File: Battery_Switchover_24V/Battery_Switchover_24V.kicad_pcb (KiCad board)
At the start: 2 copper layers, 188.9 x 89 mm, 102 parts, among them J1 USB_C_Receptacle_USB2.0_14P, J2 430450612, J4 430450612, J5 430450612, M1 Fan, Q1 PZT2222AT1G, SW1 SW_Push, U11 LM60CIM3, U12 L5973D, U13 AMS1117-3.3, U14 OPA2197xD, U2 ACS71240LLCBTR-010B3, U3 LPC11U14FBD48-201, U4 ACS37002, U5 ACS37002, U6 LM74610QDGKRQ1, U7 FDBL86066-F085, U8 ADS7830IPWR, Y1 12.000MHz

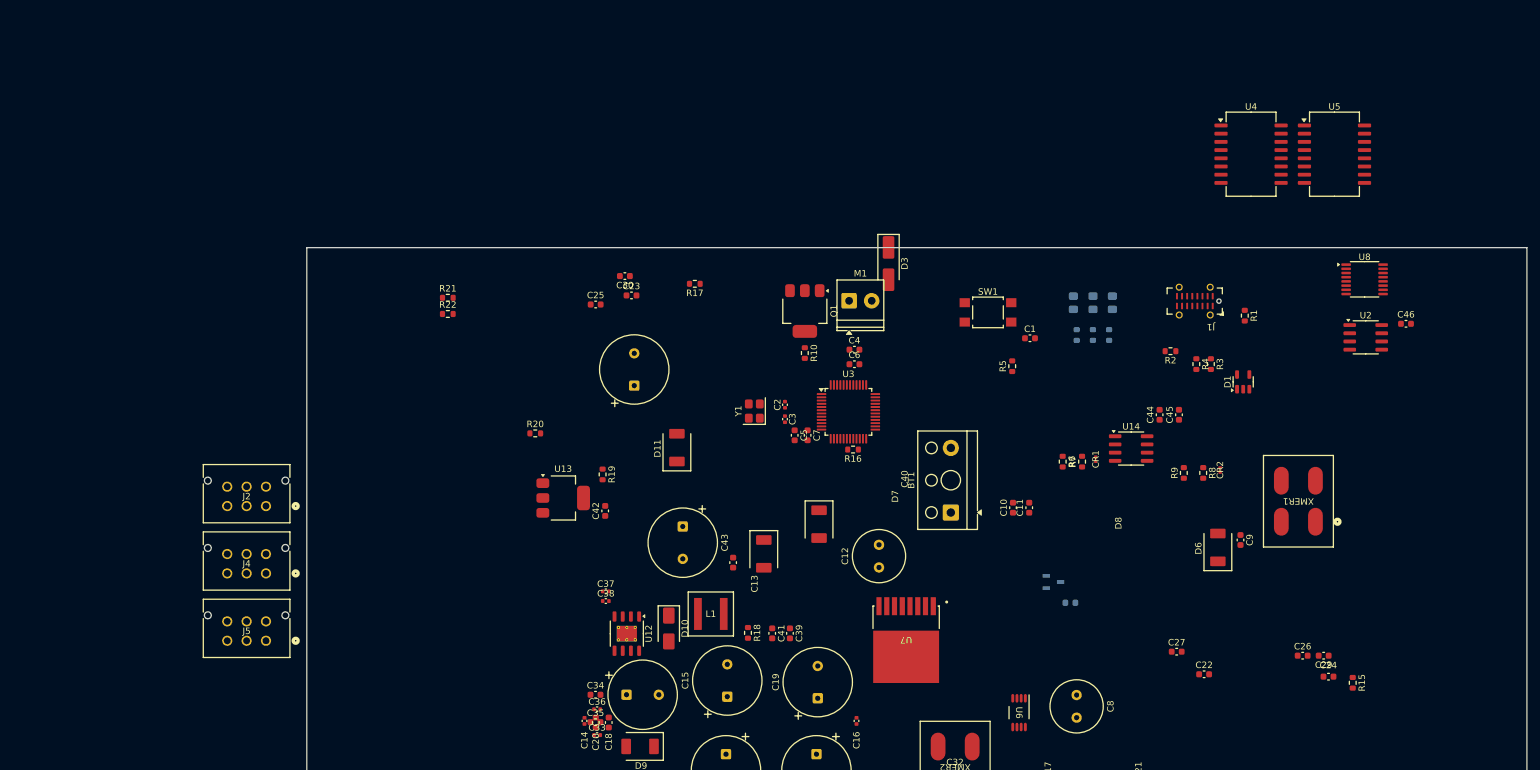
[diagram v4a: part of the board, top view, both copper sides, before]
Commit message: Batt current monitor IC added, batt moved to charger page
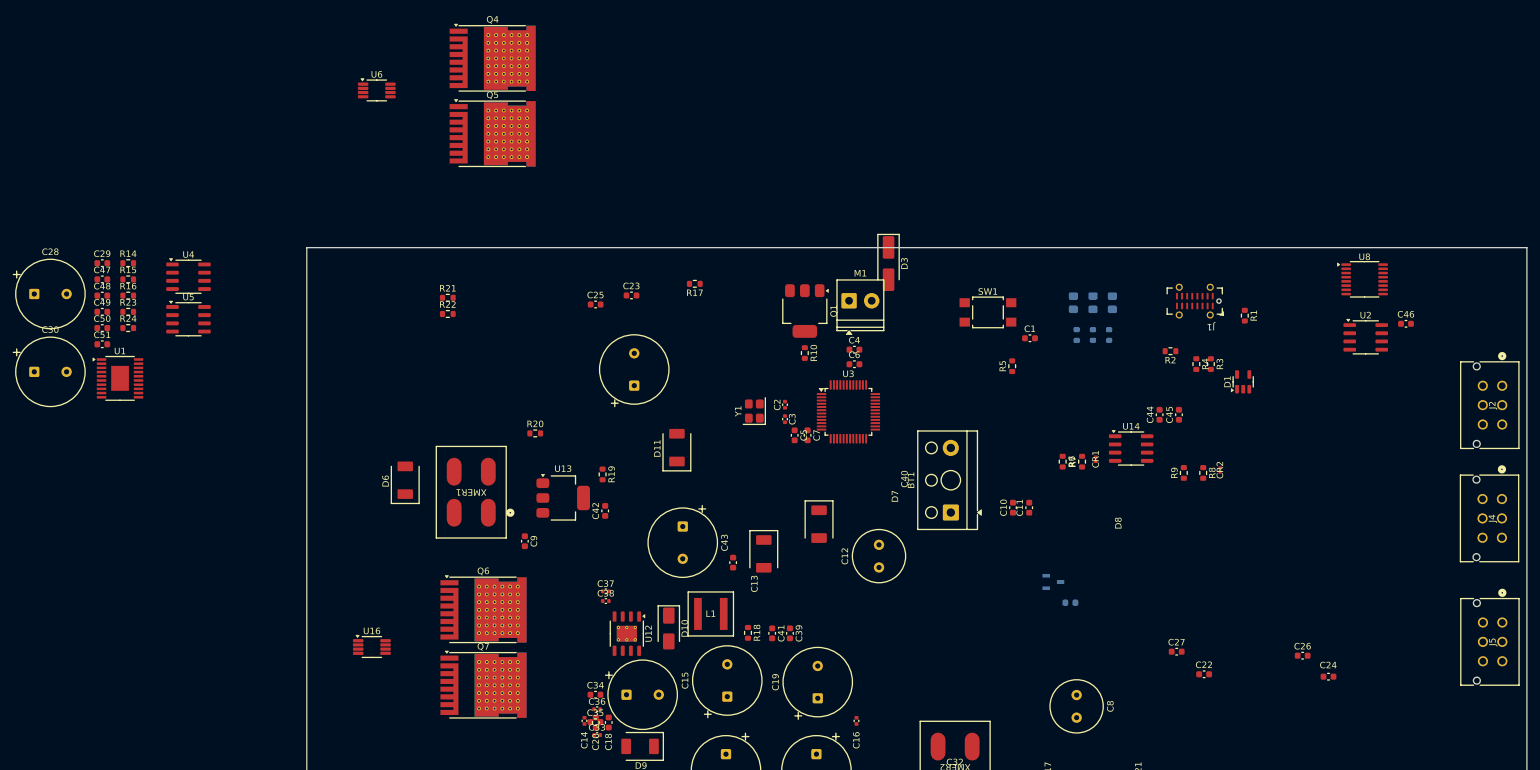
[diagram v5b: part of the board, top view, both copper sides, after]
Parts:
- removed U7: FDBL86066-F085, footprints:H-PSOF8L_ONS
- added C28: 330uF, Capacitor_THT:CP_Radial_Tantal_D10.5mm_P5.00mm, F.Cu at (47.1, 77.2)
- added C47: 100nF, Capacitor_SMD:C_0603_1608Metric, F.Cu at (57.7, 74.9)
- added C48: 100nF, Capacitor_SMD:C_0603_1608Metric, F.Cu at (57.7, 77.4)
- added C49: 100nF, Capacitor_SMD:C_0603_1608Metric, F.Cu at (57.7, 79.9)
- added C50: 100nF, Capacitor_SMD:C_0603_1608Metric, F.Cu at (57.7, 82.4)
- added C51: 100nF, Capacitor_SMD:C_0603_1608Metric, F.Cu at (57.7, 85.0)
- added Q4: FDBL86066-F085, Package_TO_SOT_SMD:Infineon_PG-HSOF-8-1_ThermalVias, F.Cu at (118.1, 40.7)
- added Q5: FDBL86066-F085, Package_TO_SOT_SMD:Infineon_PG-HSOF-8-1_ThermalVias, F.Cu at (118.1, 52.4)
- added Q6: FDBL86066-F085, Package_TO_SOT_SMD:Infineon_PG-HSOF-8-1_ThermalVias, F.Cu at (116.7, 126.1)
- added Q7: FDBL86066-F085, Package_TO_SOT_SMD:Infineon_PG-HSOF-8-1_ThermalVias, F.Cu at (116.7, 137.7)
- added R14: 7.5K, Resistor_SMD:R_0603_1608Metric, F.Cu at (61.7, 72.4)
- added R23: 7.5K, Resistor_SMD:R_0603_1608Metric, F.Cu at (61.7, 79.9)
- added R24: 7.5K, Resistor_SMD:R_0603_1608Metric, F.Cu at (61.7, 82.4)
- added U1: LM25117PSQE_NOPB, Package_SO:HTSSOP-20-1EP_4.4x6.5mm_P0.65mm_EP2.74x3.86mm, F.Cu at (60.4, 90.2)
- added U16: LM74610QDGKRQ1, Package_SO:VSSOP-8_3x3mm_P0.65mm, F.Cu at (99.4, 131.8)
- C29: value 6nF -> 100nF
- C30: value 6nF -> 330uF; footprint Capacitor_SMD:C_0603_1608Metric -> Capacitor_THT:CP_Radial_Tantal_D10.5mm_P5.00mm
- R15, R16: value 100K -> 7.5K
- U4, U5: value ACS37002 -> ACS71240LLCBTR-010B3; footprint Package_SO:SOIC-16W_7.5x12.8mm_P1.27mm -> Package_SO:SOIC-8_3.9x4.9mm_P1.27mm
- U6: footprint footprints:DGK0008A_N -> Package_SO:VSSOP-8_3x3mm_P0.65mm
- moved R15 199.5 mm to (61.7, 74.9), turned to 0 degrees
- moved C29 198.6 mm to (57.7, 72.4), turned to 0 degrees
- moved J2 192.2 mm to (274.3, 91.4), turned to 90 degrees
- moved J4 191.6 mm to (274.3, 108.9), turned to 90 degrees
- moved J5 191.4 mm to (274.4, 128.0), turned to 90 degrees
- moved U5 179.2 mm to (71.0, 81.1)
- moved U4 165.6 mm to (71.0, 74.5)
- moved U6 138.4 mm to (100.2, 45.7), turned to 0 degrees
- moved XMER1 128.0 mm to (117.4, 111.0)
- moved D6 126.2 mm to (104.5, 108.2)
- moved R16 114.7 mm to (61.7, 77.4), turned to 0 degrees
- moved C9 110.8 mm to (123.1, 115.4)
- moved C30 92.6 mm to (47.1, 89.2), turned to 0 degrees
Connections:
- C12 pad 1: Net-(U6-VCAPH) -> unconnected-(C12-Pad1)
- C12 pad 2: Net-(U6-VCAPL) -> unconnected-(C12-Pad2)
- C23 pad 2: +5V -> +3.3V
- C24 pad 2: +5V -> +3.3V
- C25 pad 2: VREF3 -> Net-(U5-ERR/FILTER)
- C26 pad 2: VREF2 -> Net-(U4-ERR/FILTER)
- C29 pad 1: GND -> Net-(D13-K)
- C29 pad 2: VIOUT2 -> Net-(U1-SW)
- C30 pad 1: GND -> Net-(D13-A)
- C30 pad 2: VIOUT3 -> GND
- R15 pad 1: +5V -> GND
- R15 pad 2: Net-(U4-*OCF) -> Net-(U1-UVLO)
- R16 pad 1: +5V -> Net-(U1-RAMP)
- R16 pad 2: Net-(U5-*OCF) -> unconnected-(R16-Pad2)
- U4 pad 3: Load2 -> GNDPWR2
- U4 pad 4: Load2 -> GNDPWR2
- U4 pad 5: GNDPWR2 -> GND
- U4 pad 6: GNDPWR2 -> Net-(U4-ERR/FILTER)
- U4 pad 7: GNDPWR2 -> VIOUT2
- U4 pad 8: GNDPWR2 -> +3.3V
- U5 pad 3: Load3 -> GNDPWR3
- U5 pad 4: Load3 -> GNDPWR3
- U5 pad 5: GNDPWR3 -> GND
- U5 pad 6: GNDPWR3 -> Net-(U5-ERR/FILTER)
- U5 pad 7: GNDPWR3 -> VIOUT3
- U5 pad 8: GNDPWR3 -> +3.3V
- U6 pad 1: Net-(U6-VCAPL) -> unconnected-(U6-VCAPL-Pad1)
- U6 pad 2: Net-(U6-GATE_DRIVE) -> unconnected-(U6-GATE_PULL_DOWN-Pad2)
- U6 pad 4: Vbatt -> unconnected-(U6-ANODE-Pad4)
- U6 pad 6: Net-(U6-GATE_DRIVE) -> unconnected-(U6-GATE_DRIVE-Pad6)
- U6 pad 7: Net-(U6-VCAPH) -> unconnected-(U6-VCAPH-Pad7)
- U6 pad 8: Net-(U6-CATHODE) -> unconnected-(U6-CATHODE-Pad8)
- U8 pad 1: VIOUT1 -> Net-(RN1-R1.2)
- U8 pad 2: unconnected-(U8-CH1-Pad2) -> Net-(RN1-R2.2)
- U8 pad 3: unconnected-(U8-CH2-Pad3) -> Net-(RN1-R3.2)
- U8 pad 4: unconnected-(U8-CH3-Pad4) -> Net-(RN1-R4.2)
- U8 pad 5: unconnected-(U8-CH4-Pad5) -> Net-(RN2-R1.2)
- U8 pad 6: unconnected-(U8-CH5-Pad6) -> Net-(RN2-R2.2)
- U8 pad 7: unconnected-(U8-CH6-Pad7) -> Net-(RN2-R3.2)
- XMER2 pad 1: Net-(U6-CATHODE) -> unconnected-(XMER2-Pad1)

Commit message: Cap FP, Choke FP, Ind FP added. Basic locations
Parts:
- added C52: 6nF, Capacitor_SMD:C_0603_1608Metric, F.Cu at (227.2, -13.0)
- added C53: 100nF, Capacitor_SMD:C_0603_1608Metric, F.Cu at (227.2, -10.5)
- added C54: 1nF, Capacitor_SMD:C_1206_3216Metric, F.Cu at (146.3, 94.1)
- added C55: 1nF, Capacitor_SMD:C_1206_3216Metric, F.Cu at (146.3, 97.0)
- added C56: 1nF, Capacitor_SMD:C_1206_3216Metric, F.Cu at (112.7, 114.3)
- added C57: 330uF, Capacitor_THT:CP_Radial_Tantal_D10.5mm_P5.00mm, F.Cu at (214.6, -30.7)
- added C58: 10nF, Capacitor_SMD:C_1206_3216Metric, F.Cu at (114.3, 75.6)
- added C59: 330uF, Capacitor_THT:CP_Radial_Tantal_D10.5mm_P5.00mm, F.Cu at (214.6, -18.7)
- added C60: 100nF, Capacitor_SMD:C_1206_3216Metric, F.Cu at (114.4, 78.6)
- added C61: 330uF, Capacitor_THT:CP_Radial_Tantal_D10.5mm_P5.00mm, F.Cu at (96.6, 141.1)
- added C62: 100nF, Capacitor_SMD:C_0603_1608Metric, F.Cu at (227.2, 19.0)
- added D14: P6SMBJ26A, Diode_SMD:D_SMB_Handsoldering, F.Cu at (132.3, 104.9)
- added D15: ESDA5V3SC5, Package_TO_SOT_SMD:SOT-23-5, F.Cu at (249.8, 82.7)
- added J10: ATX_2X3, Connector_Molex:Molex_Mini-Fit_Jr_5566-06A_2x03_P4.20mm_Vertical, F.Cu at (101.9, 107.7)
- added J11: ATX_2X3, Connector_Molex:Molex_Mini-Fit_Jr_5566-06A_2x03_P4.20mm_Vertical, F.Cu at (116.8, 107.7)
- added J12: ATX_2X3, Connector_Molex:Molex_Mini-Fit_Jr_5566-06A_2x03_P4.20mm_Vertical, F.Cu at (116.8, 128.1)
- added J13: ATX_2X3, Connector_Molex:Molex_Mini-Fit_Jr_5566-06A_2x03_P4.20mm_Vertical, F.Cu at (101.9, 128.2)
- added J6: Conn_01x08, TerminalBlock_Phoenix:TerminalBlock_Phoenix_PT-1,5-8-3.5-H_1x08_P3.50mm_Horizontal, F.Cu at (255.6, 75.4)
- added J8: ATX_2X3, Connector_Molex:Molex_Mini-Fit_Jr_5566-06A_2x03_P4.20mm_Vertical, F.Cu at (116.8, 89.6)
- added J9: ATX_2X3, Connector_Molex:Molex_Mini-Fit_Jr_5566-06A_2x03_P4.20mm_Vertical, F.Cu at (101.9, 89.6)
- added L2: L, Inductor_SMD:L_Vishay_IHLP-6767, F.Cu at (193.8, 116.1)
- added Q2: PJD50N10AL_L2, Package_TO_SOT_SMD:TO-252-2, F.Cu at (214.9, 97.7)
- added Q3: PJD50N10AL_L2, Package_TO_SOT_SMD:TO-252-2, F.Cu at (214.9, 104.9)
- added R25: 7.5K, Resistor_SMD:R_0603_1608Metric, F.Cu at (227.2, -8.02)
- added R26: 7.5K, Resistor_SMD:R_0603_1608Metric, F.Cu at (227.2, -5.51)
- added R27: 7.5K, Resistor_SMD:R_0603_1608Metric, F.Cu at (227.2, -3.00)
- added R28: 2K, Resistor_SMD:R_0603_1608Metric, F.Cu at (227.2, -25.1)
- added R29: 10K, Resistor_SMD:R_0603_1608Metric, F.Cu at (231.2, -37.6)
- added R30: 1K, Resistor_SMD:R_0603_1608Metric, F.Cu at (231.2, -35.1)
- added R31: 1K, Resistor_SMD:R_0603_1608Metric, F.Cu at (231.2, -32.6)
- added R32: 2K, Resistor_SMD:R_0603_1608Metric, F.Cu at (231.2, -30.1)
- added R33: 1K, Resistor_SMD:R_0603_1608Metric, F.Cu at (231.2, -27.6)
- added R34: 3K, Resistor_SMD:R_0603_1608Metric, F.Cu at (231.2, -25.1)
- added R35: 0, Resistor_SMD:R_0603_1608Metric, F.Cu at (235.2, -37.6)
- added R36: 1K, Resistor_SMD:R_0603_1608Metric, F.Cu at (235.2, -35.1)
- added R37: 2K, Resistor_SMD:R_0603_1608Metric, F.Cu at (235.2, -32.6)
- added R38: 1K, Resistor_SMD:R_0603_1608Metric, F.Cu at (235.2, -30.1)
- added R39: 10R, Resistor_SMD:R_0603_1608Metric, F.Cu at (235.2, -27.6)
- added R40: 0, Resistor_SMD:R_0603_1608Metric, F.Cu at (235.2, -25.1)
- added R41: 2K, Resistor_SMD:R_0603_1608Metric, F.Cu at (239.2, -37.6)
- added R42: 12K, Resistor_SMD:R_0603_1608Metric, F.Cu at (239.2, -35.1)
- added R43: 2K, Resistor_SMD:R_0603_1608Metric, F.Cu at (239.2, -32.6)
- added R44: 1K, Resistor_SMD:R_0603_1608Metric, F.Cu at (239.2, -30.1)
- added R45: 1K, Resistor_SMD:R_0603_1608Metric, F.Cu at (239.2, -27.6)
- added R46: 1K, Resistor_SMD:R_0603_1608Metric, F.Cu at (239.2, -25.1)
- added U7: ACS71240LLCBTR-010B3, Package_SO:SOIC-8_3.9x4.9mm_P1.27mm, F.Cu at (201.1, 89.6)
- added U9: LMV321, Package_TO_SOT_SMD:SOT-23-5_HandSoldering, F.Cu at (192.6, 89.0)
- C10: value 1nF -> 100pF; footprint Capacitor_SMD:C_0603_1608Metric -> Capacitor_SMD:C_1206_3216Metric
- C11: footprint Capacitor_SMD:C_0603_1608Metric -> Capacitor_SMD:C_1206_3216Metric
- C12, C8: footprint Capacitor_THT:C_Radial_D8.0mm_H7.0mm_P3.50mm -> Capacitor_SMD:C_0805_2012Metric
- C13: value 100pF -> 330uF; footprint Capacitor_SMD:C_0603_1608Metric -> Capacitor_THT:CP_Radial_Tantal_D10.5mm_P5.00mm
- C14, C16: value 1nF -> 100nF; footprint Capacitor_SMD:C_0402_1005Metric -> Capacitor_SMD:C_0603_1608Metric
- C15: value 330uF -> 100nF; footprint Capacitor_THT:CP_Radial_Tantal_D10.5mm_P5.00mm -> Capacitor_SMD:C_0603_1608Metric
- C17: value 330uF -> 100n; footprint Capacitor_THT:CP_Radial_Tantal_D10.5mm_P5.00mm -> Capacitor_SMD:C_0603_1608Metric
- C18: value 10nF -> 10u
- C19, C21: value 330uF -> 10nF; footprint Capacitor_THT:CP_Radial_Tantal_D10.5mm_P5.00mm -> Capacitor_SMD:C_0603_1608Metric
- C20: value 100nF -> 10nF
- C32, C40, C43: footprint Capacitor_THT:CP_Radial_Tantal_D10.5mm_P5.00mm -> Capacitor_SMD:CP_Elec_8x10
- C46: value 100nF -> 100n
- D6, D7: footprint footprints:P26_DO-214AA_SMB -> Diode_SMD:D_SMB_Handsoldering
- D8: value P6SMBJ26A -> ESDA5V3SC5; footprint footprints:P26_DO-214AA_SMB -> Package_TO_SOT_SMD:SOT-23-5
- J2, J4, J5: value 430450612 -> M8; footprint footprints:CONN_SD-43045-005_06_MOL -> M8_Screw_Terminal:M8_Screw_Terminal; moved to B.Cu
- XMER1, XMER2: footprint footprints:CM5441Z101B-10_LRD -> Inductor_THT:Choke_Schaffner_RN116-04-22.5x21.5mm
- moved C18 200.5 mm to (227.2, -35.1), turned to 0 degrees
- moved C17 199.8 mm to (227.2, -37.6), turned to 0 degrees
- moved C20 197.0 mm to (227.2, -30.1), turned to 0 degrees
- moved C14 189.3 mm to (227.2, -20.6), turned to 0 degrees
- moved C21 185.6 mm to (227.2, -27.6), turned to 0 degrees
- moved C19 182.1 mm to (227.2, -32.6), turned to 0 degrees
- moved C15 173.5 mm to (227.2, -18.1), turned to 0 degrees
- moved C13 172.1 mm to (214.6, -42.8), turned to 0 degrees
- moved C2 169.5 mm to (166.4, 263.7)
- moved C22 169.5 mm to (231.3, 305.5)
- moved C25 169.5 mm to (137.1, 248.2)
- moved C27 169.5 mm to (227.1, 302.0)
- moved C3 169.5 mm to (166.4, 266.0)
- moved C31 169.5 mm to (210.6, 294.4)
- moved C33 169.5 mm to (137.3, 314.9)
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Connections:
- net Fan_Control renamed FAN_CONTROL
- net Load3 renamed LOAD3_GND_RETURN
- net Temp_data renamed BATTERY_OW_TEMP
- BT1 pad 1: Vbatt -> VBATT
- BT1 pad 2: GND -> Net-(BT1--)
- C10 pad 1: Vbatt -> Net-(D7-A2)
- C11 pad 1: Vbatt -> VOUT
- C11 pad 2: GND -> VOUT_GNDPWR
- C12 pad 1: unconnected-(C12-Pad1) -> Net-(U6-VCAPH)
- C12 pad 2: unconnected-(C12-Pad2) -> Net-(U6-VCAPL)
- C13 pad 1: Vbatt -> VOUT
- C13 pad 2: GND -> VOUT_GNDPWR
- C14 pad 1: Vsupply -> VBATT
- C15 pad 1: Vsupply -> VBATT
- C16 pad 1: Vsupply -> GND
- C16 pad 2: GND -> +3.3V
- C17 pad 1: Vsupply -> GND
- C17 pad 2: GND -> Net-(U8-REFin/REFout)
- C18 pad 1: Vsupply -> GND
- C18 pad 2: GND -> Net-(U8-VDD)
- C19 pad 1: Vsupply -> GND
- C19 pad 2: GND -> VIOUT1
- C20 pad 1: Vsupply -> GND
- C20 pad 2: GND -> VIOUT2
- C21 pad 1: Vsupply -> GND
- C21 pad 2: GND -> VIOUT3
- C28 pad 1: BATT -> VBATT
- C32 pad 1: Vsupply -> VOUT
- C33 pad 2: Vsupply -> VOUT
- C34 pad 2: Vsupply -> VOUT
- C35 pad 2: Vsupply -> VOUT
- C36 pad 2: Vsupply -> VOUT
- C46 pad 2: +5V -> Net-(U8-VDD)
- C8 pad 1: unconnected-(C8-Pad1) -> Net-(U16-VCAPH)
- C8 pad 2: unconnected-(C8-Pad2) -> Net-(U16-VCAPL)
- C9 pad 1: Net-(C9-Pad1) -> VIN
- D3 pad 1: Vsupply -> VOUT
- D6 pad 1: GND -> Net-(D6-A1)
- D6 pad 2: Vin -> Net-(D6-A2)
- D7 pad 2: Vbatt -> Net-(D7-A2)
- D8 pad 1: GND -> Net-(U8-CH0)
- D8 pad 2: Vsupply -> GND
- D9 pad 2: Vsupply -> VOUT
- J2 pad 1: GND -> Net-(J2-Pin_1)
- J4 pad 1: GND -> Net-(D6-A1)
- J5 pad 1: GND -> Net-(D6-A2)
- M1 pad 1: Vsupply -> VOUT
- R14 pad 1: Net-(U1-VIN) -> VIN
- U1 pad 20: Net-(U1-VIN) -> VIN
- U11 pad 2: V_temp -> BOARD_TEMPERATURE
- U12 pad 8: Vsupply -> VOUT
- U16 pad 1: unconnected-(U16-VCAPL-Pad1) -> Net-(U16-VCAPL)
- U16 pad 2: unconnected-(U16-GATE_PULL_DOWN-Pad2) -> Net-(U16-GATE_DRIVE)
- U16 pad 4: unconnected-(U16-ANODE-Pad4) -> VIN
- U16 pad 6: unconnected-(U16-GATE_DRIVE-Pad6) -> Net-(U16-GATE_DRIVE)
- U16 pad 7: unconnected-(U16-VCAPH-Pad7) -> Net-(U16-VCAPH)
- U16 pad 8: unconnected-(U16-CATHODE-Pad8) -> Net-(D7-A2)
- U2 pad 1: Load2 -> LOAD1_GND_RETURN
- U2 pad 2: Load2 -> LOAD1_GND_RETURN
- U2 pad 3: GNDPWR1 -> VOUT_GNDPWR
- U2 pad 4: GNDPWR1 -> VOUT_GNDPWR
- U2 pad 7: VIOUT1 -> Net-(U2-VIOUT)
- U3 pad 34: VREF3 -> unconnected-(U3-PIO0_13-Pad34)
- U3 pad 39: VREF3 -> unconnected-(U3-PIO0_15-Pad39)
- U3 pad 45: VREF3 -> unconnected-(U3-PIO0_17-Pad45)
- U4 pad 1: Load2 -> LOAD2_GND_RETURN
- U4 pad 2: Load2 -> LOAD2_GND_RETURN
- U4 pad 3: GNDPWR2 -> VOUT_GNDPWR
- U4 pad 4: GNDPWR2 -> VOUT_GNDPWR
- U4 pad 7: VIOUT2 -> Net-(U4-VIOUT)
- U5 pad 3: GNDPWR3 -> VOUT_GNDPWR
- U5 pad 4: GNDPWR3 -> VOUT_GNDPWR
- U5 pad 7: VIOUT3 -> Net-(U5-VIOUT)
- U6 pad 1: unconnected-(U6-VCAPL-Pad1) -> Net-(U6-VCAPL)
- U6 pad 2: unconnected-(U6-GATE_PULL_DOWN-Pad2) -> Net-(U6-GATE_DRIVE)
- U6 pad 4: unconnected-(U6-ANODE-Pad4) -> VBATT
- U6 pad 6: unconnected-(U6-GATE_DRIVE-Pad6) -> Net-(U6-GATE_DRIVE)
- U6 pad 7: unconnected-(U6-VCAPH-Pad7) -> Net-(U6-VCAPH)
- U6 pad 8: unconnected-(U6-CATHODE-Pad8) -> Net-(D7-A2)
- U8 pad 1: Net-(RN1-R1.2) -> Net-(U8-CH0)
- U8 pad 10: unconnected-(U8-REFin/REFout-Pad10) -> Net-(U8-REFin/REFout)
- U8 pad 11: unconnected-(U8-COM-Pad11) -> Net-(U8-COM)
- U8 pad 16: +5V -> Net-(U8-VDD)
- U8 pad 2: Net-(RN1-R2.2) -> Net-(U8-CH1)
- U8 pad 3: Net-(RN1-R3.2) -> Net-(U8-CH2)
- U8 pad 4: Net-(RN1-R4.2) -> Net-(U8-CH3)
- U8 pad 8: unconnected-(U8-CH7-Pad8) -> Net-(U8-CH7)
- XMER1 pad 1: Vin -> Net-(D6-A2)
- XMER1 pad 2: GND -> Net-(D6-A1)
- XMER1 pad 4: Net-(C9-Pad1) -> VIN
- XMER2 pad 1: unconnected-(XMER2-Pad1) -> Net-(D7-A2)
- XMER2 pad 3: GND -> VOUT_GNDPWR
- XMER2 pad 4: Vsupply -> VOUT

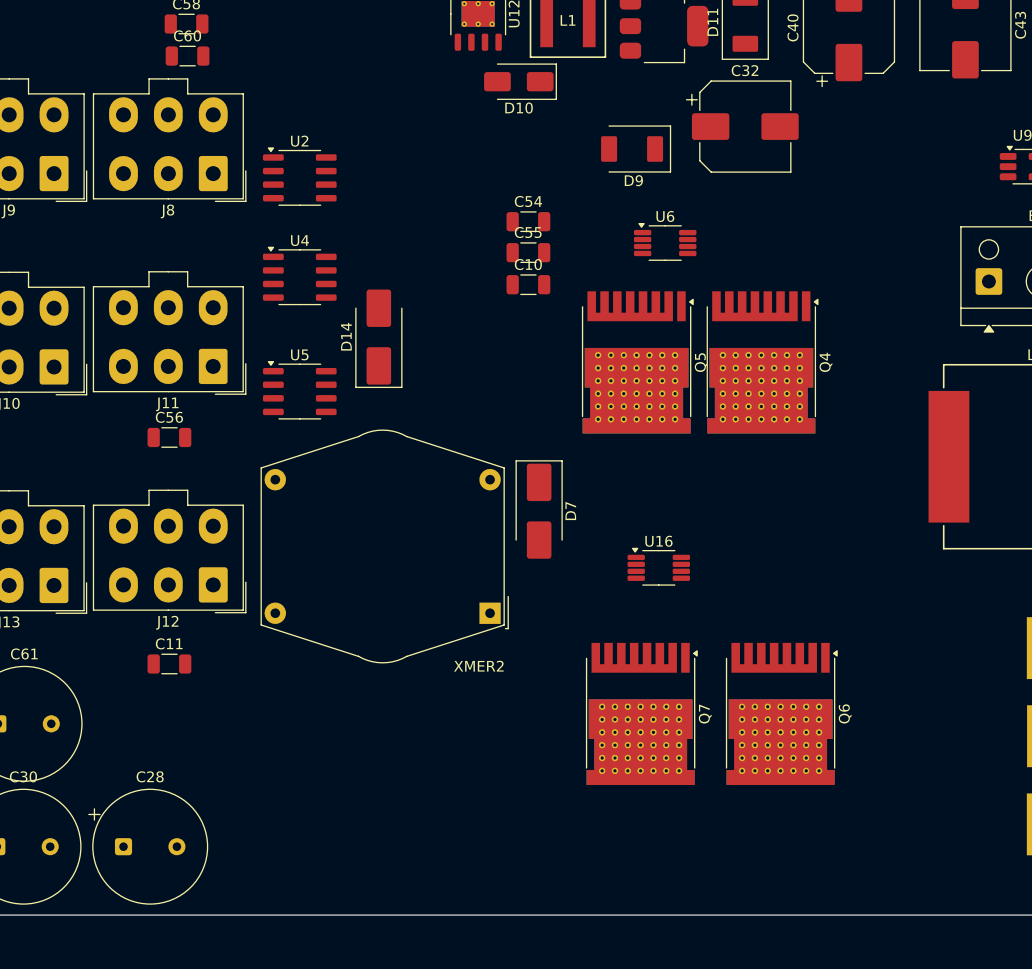
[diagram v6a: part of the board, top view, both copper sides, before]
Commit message: Cm choke model and docs
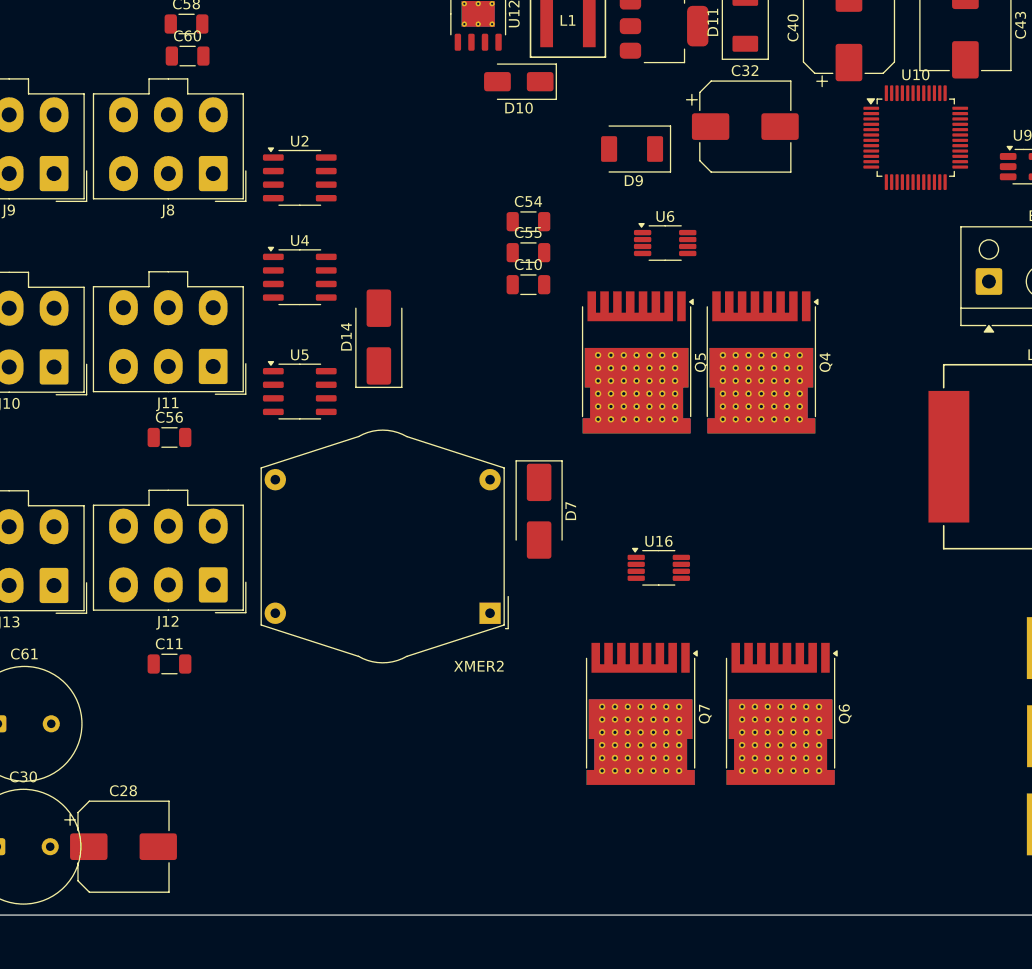
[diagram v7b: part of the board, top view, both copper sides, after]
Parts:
- added U10: LPC11U67JBD48, Package_QFP:LQFP-48_7x7mm_P0.5mm, F.Cu at (182.6, 86.2)
- C28: footprint Capacitor_THT:CP_Radial_Tantal_D10.5mm_P5.00mm -> Capacitor_SMD:CP_Elec_8x10
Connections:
- C2 pad 2: Net-(U3-XTALIN) -> Net-(C2-Pad2)
- C3 pad 2: Net-(U3-XTALOUT) -> Net-(C3-Pad2)
- D1 pad 3: Net-(U3-USB_DP) -> Net-(D1-K-Pad3)
- D1 pad 4: Net-(U3-USB_DM) -> Net-(D1-K-Pad4)
- R3 pad 2: Net-(U3-USB_DM) -> Net-(D1-K-Pad4)
- R4 pad 2: Net-(U3-USB_DP) -> Net-(D1-K-Pad3)
- U3 pad 13: Battery_Status_LED -> unconnected-(U3-PIO1_20-Pad13)
- U3 pad 14: PI003 -> unconnected-(U3-PIO0_3-Pad14)
- U3 pad 15: SCL -> unconnected-(U3-PIO0_4-Pad15)
- U3 pad 16: SDA -> unconnected-(U3-PIO0_5-Pad16)
- U3 pad 18: BATTERY_OW_TEMP -> unconnected-(U3-PIO1_23-Pad18)
- U3 pad 19: Net-(U3-USB_DM) -> unconnected-(U3-USB_DM-Pad19)
- U3 pad 2: Main_Voltage_LED -> unconnected-(U3-PIO1_19-Pad2)
- U3 pad 20: Net-(U3-USB_DP) -> unconnected-(U3-USB_DP-Pad20)
- U3 pad 26: Fan_Status_LED -> unconnected-(U3-PIO1_21-Pad26)
- U3 pad 29: V_temp -> unconnected-(U3-PIO0_10-Pad29)
- U3 pad 3: RESET -> unconnected-(U3-PIO0_0-Pad3)
- U3 pad 32: ADC_In -> unconnected-(U3-PIO0_11-Pad32)
- U3 pad 33: ADC_Batt -> unconnected-(U3-PIO0_12-Pad33)
- U3 pad 35: VIOUT1 -> unconnected-(U3-PIO0_14-Pad35)
- U3 pad 40: VIOUT2 -> unconnected-(U3-PIO0_16-Pad40)
- U3 pad 41: GND -> unconnected-(U3-VSS-Pad41)
- U3 pad 42: FAN_CONTROL -> unconnected-(U3-PIO0_23-Pad42)
- U3 pad 44: +3.3V -> unconnected-(U3-VDD-Pad44)
- U3 pad 46: VIOUT3 -> unconnected-(U3-PIO0_18-Pad46)
- U3 pad 5: GND -> unconnected-(U3-VSS-Pad5)
- U3 pad 6: Net-(U3-XTALIN) -> unconnected-(U3-XTALIN-Pad6)
- U3 pad 7: Net-(U3-XTALOUT) -> unconnected-(U3-XTALOUT-Pad7)
- U3 pad 8: +3.3V -> unconnected-(U3-VDD-Pad8)
- Y1 pad 1: Net-(U3-XTALOUT) -> Net-(C3-Pad2)
- Y1 pad 2: Net-(U3-XTALIN) -> Net-(C2-Pad2)
